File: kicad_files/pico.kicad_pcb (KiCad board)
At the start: 2 copper layers, 100 x 98 mm, 74 parts, among them K0 KEYSW, K1 KEYSW, K10 KEYSW, K11 KEYSW, K12 KEYSW, K13 KEYSW, K14 KEYSW, K15 KEYSW, K2 KEYSW, K20 KEYSW, K21 KEYSW, K22 KEYSW, K23 KEYSW, K24 KEYSW, K25 KEYSW, K3 KEYSW, K30 KEYSW, K31 KEYSW, K32 KEYSW, K33 KEYSW, K34 KEYSW, K35 KEYSW, K4 KEYSW, K40 KEYSW, K41 KEYSW, K42 KEYSW, K43 KEYSW, K44 KEYSW, K45 KEYSW, K5 KEYSW, U1 ProMicro

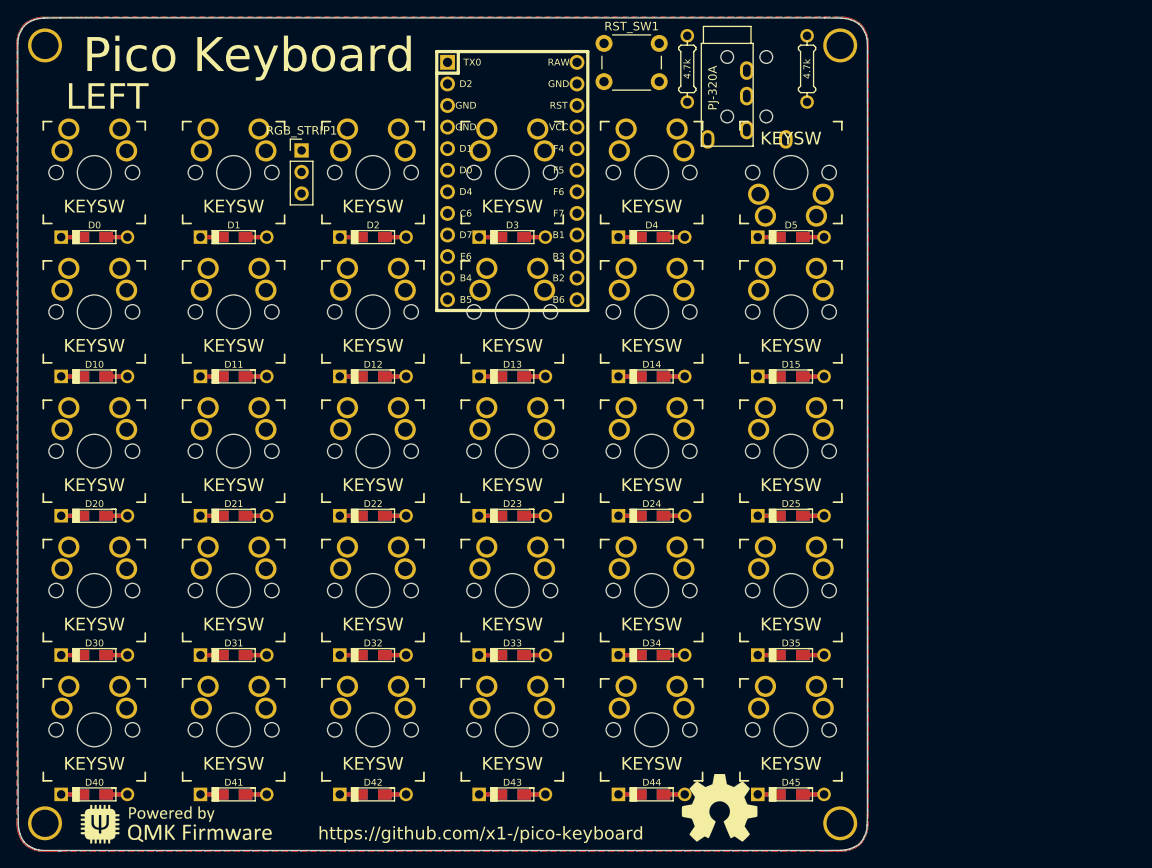
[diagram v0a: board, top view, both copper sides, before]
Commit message: Modified outline of pico keyboard.
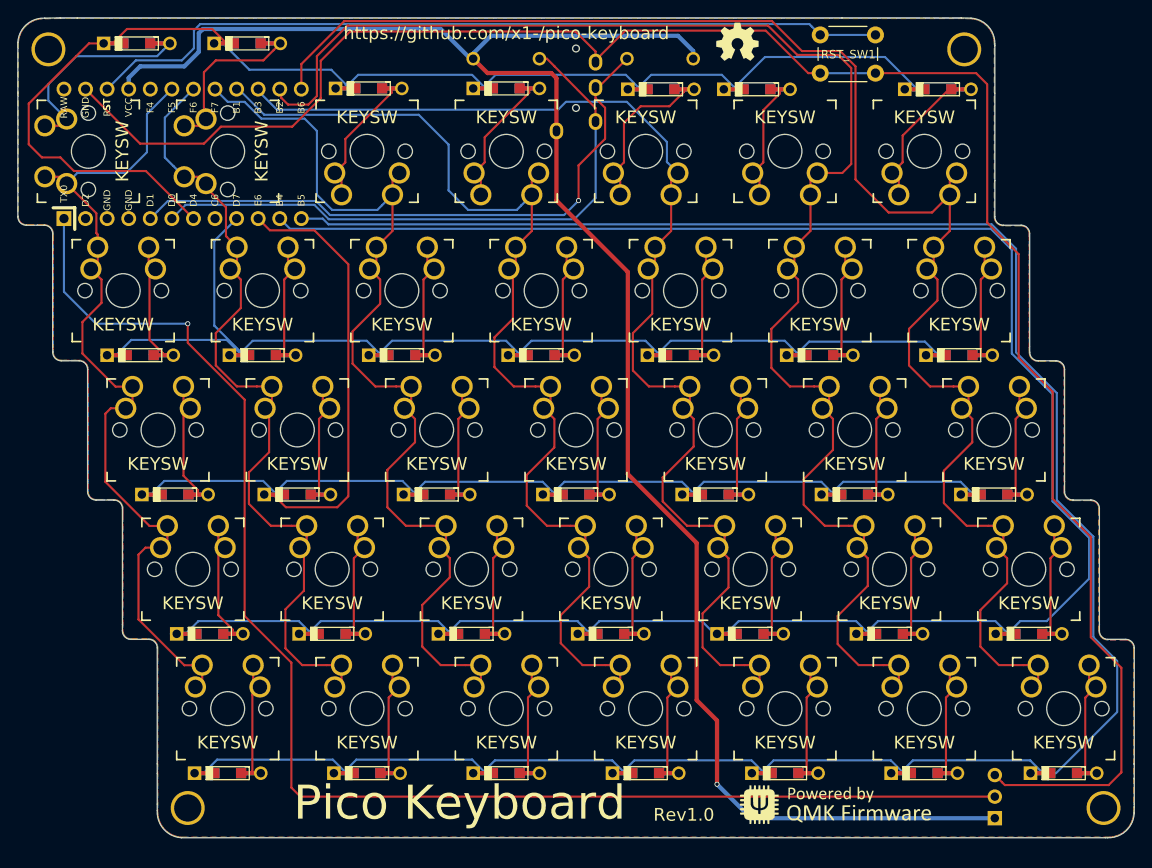
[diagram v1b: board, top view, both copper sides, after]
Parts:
- removed the REF*** at (164.6, 140.0)
- added D16: D, pico_footprints:Diode-dual, F.Cu at (192.8, 86.7)
- added D26: D, pico_footprints:Diode-dual, F.Cu at (196.9, 103.1)
- added D36: D, pico_footprints:Diode-dual, F.Cu at (201.0, 119.5)
- added D46: D, pico_footprints:Diode-dual, F.Cu at (205.1, 135.9)
- added D6: D, pico_footprints:Diode-dual, F.Cu at (190.3, 55.4)
- added K16: KEYSW, pico_footprints:Kailh_mid_height, F.Cu at (192.8, 79.1)
- added K26: KEYSW, pico_footprints:Kailh_mid_height, F.Cu at (196.9, 95.5)
- added K36: KEYSW, pico_footprints:Kailh_mid_height, F.Cu at (201.0, 111.9)
- added K46: KEYSW, pico_footprints:Kailh_mid_height, F.Cu at (205.1, 128.3)
- added K6: KEYSW, pico_footprints:Kailh_mid_height, F.Cu at (188.7, 62.7)
- added REF***: OSHW-Logo2_14.6x12mm_SilkScreen, pico_footprints:OSHW_logo_silkscreen-front_5mm, F.Cu at (166.7, 49.8)
- D0, D1, D10, D11, D12, D13, D14, D15, D2, D20, D21, D22, D23, D24, D25, D3, D30, D31, D32, D33, D34, D35, D4, D40, D41, D42, D43, D44, D45, D5: footprint Keebio-Parts:Diode-dual -> pico_footprints:Diode-dual
- R1, R2: footprint Keebio-Parts:Resistor-Compact -> pico_footprints:Resistor-Compact
- REF***: footprint Symbols:OSHW-Symbol_8.9x8mm_SilkScreen -> pico_footprints:OSHW_logo_silkscreen-front_5mm
- RGB_STRIP1: footprint Pin_Headers:Pin_Header_Straight_1x03_Pitch2.54mm -> pico_footprints:Pin_Header_Straight_1x03_Pitch2.54mm
- RST_SW1: footprint Buttons_Switches_ThroughHole:SW_PUSH_6mm_h4.3mm -> pico_footprints:SW_PUSH_6mm_h4.3mm
- TRRS1: footprint Keebio-Parts:TRRS-PJ-320A-dual -> pico_footprints:TRRS-PJ-320A
- U1: footprint Keebio-Parts:ArduinoProMicro -> pico_footprints:ArduinoProMicro
- moved RGB_STRIP1 113.3 mm to (197.0, 141.2), turned to 180 degrees
- moved REF*** 112.9 mm to (166.7, 49.8)
- moved G*** 77.6 mm to (178.3, 139.6)
- moved G*** 40.2 mm to (123.4, 139.6)
- moved U1 38.9 mm to (101.4, 63.0), turned to 0 degrees
- moved HOLE_M3 31.2 mm to (209.9, 139.9)
- moved RST_SW1 25.5 mm to (176.4, 49.0)
- moved D0 23.3 mm to (96.0, 50.0)
- moved D1 22.9 mm to (109.0, 50.0)
- moved R2 21.3 mm to (139.5, 51.8), turned to 0 degrees
- moved TRRS1 20.1 mm to (147.7, 49.0)
- moved D5 17.9 mm to (169.0, 55.4)
- moved D3 17.5 mm to (139.5, 55.3)
- moved D2 17.5 mm to (123.3, 55.3)
- moved D4 17.4 mm to (157.7, 55.4)
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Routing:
- net row4: track 0.00 -> 278.2 mm
- net row3: track 0.00 -> 261.3 mm
- net GND: track 0.00 -> 226.9 mm
- net VCC: track 0.00 -> 212.1 mm, vias 0 -> 1
- net col6: track 0.00 -> 184.4 mm
- net col5: track 0.00 -> 178.6 mm
- net row2: track 0.00 -> 170.2 mm
- net rgb_data: track 0.00 -> 167.6 mm, vias 0 -> 1
- net row0: track 0.00 -> 162.4 mm
- net col4: track 0.00 -> 140.4 mm
- net row1: track 0.00 -> 138.2 mm
- net col3: track 0.00 -> 128.6 mm
- net col2: track 0.00 -> 117.0 mm
- net col0: track 0.00 -> 103.4 mm
- net col1: track 0.00 -> 97.5 mm
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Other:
- board size 100 x 98 mm -> 131.4 x 96.5 mm
- board text added: "Mounting Surface"
- board text added: "Rev1.0"
- board text removed: "LEFT"
- board text removed: "RIGHT"

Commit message: Modified sign of schematic.
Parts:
- moved REF*** 5.40 mm to (172.1, 49.6)
- moved REF*** 1.82 mm to (168.5, 49.5)
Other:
- board text added: "https://github.com/kumaokobo/pico-keyboard"
- board text removed: "https://github.com/x1-/pico-keyboard"
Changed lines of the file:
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@@
   (title_block
     (title "Pico Keyboard PCB")
-    (date 2019-09-01)
+    (date 2019-11-01)
     (rev 1.0)
     (comment 1 "designed by x1")
-    (comment 2 https://github.com/x1-/pico-keyboard)
+    (comment 2 https://github.com/kumaokobo/pico-keyboard)
   )
   (layers
@@
   )
   (module pico_footprints:OSHW_logo_silkscreen-front_5mm (layer B.Cu)
-    (at 166.7 49.76 180)
+    (at 168.5 49.46 180)
     (fp_text reference REF*** (at -0.6 -0.2 180) (layer F.SilkS) hide
       (effects (font (size 1 1) (thickness 0.15)))
@@
   )
   (module pico_footprints:OSHW_logo_silkscreen-front_5mm (layer F.Cu)
-    (at 166.7 49.76)
+    (at 172.1 49.56)
     (fp_text reference REF*** (at -0.6 0.2) (layer F.SilkS) hide
       (effects (font (size 1 1) (thickness 0.15)))
@@
     (effects (font (size 4 4) (thickness 0.75)))
   )
-  (gr_text https://github.com/x1-/pico-keyboard (at 139.5 48.76) (layer F.SilkS)
+  (gr_text https://github.com/kumaokobo/pico-keyboard (at 141.7 48.66) (layer F.SilkS)
     (effects (font (size 1.5 1.5) (thickness 0.3)))
   )
